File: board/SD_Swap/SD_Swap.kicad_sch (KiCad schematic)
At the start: 43 parts, among them J1 USB_C, Q1 Q_Dual_PNP_PNP_E1B1C2E2B2C1, U1 74LVC2G14, U2 RTS5306E, U3 PCB_SD, U4 93AAxxAT, U5 TS3A27518ERTW, U6 SD_SOCKET, U7 AZ1117-3.3, Y1 12MHz

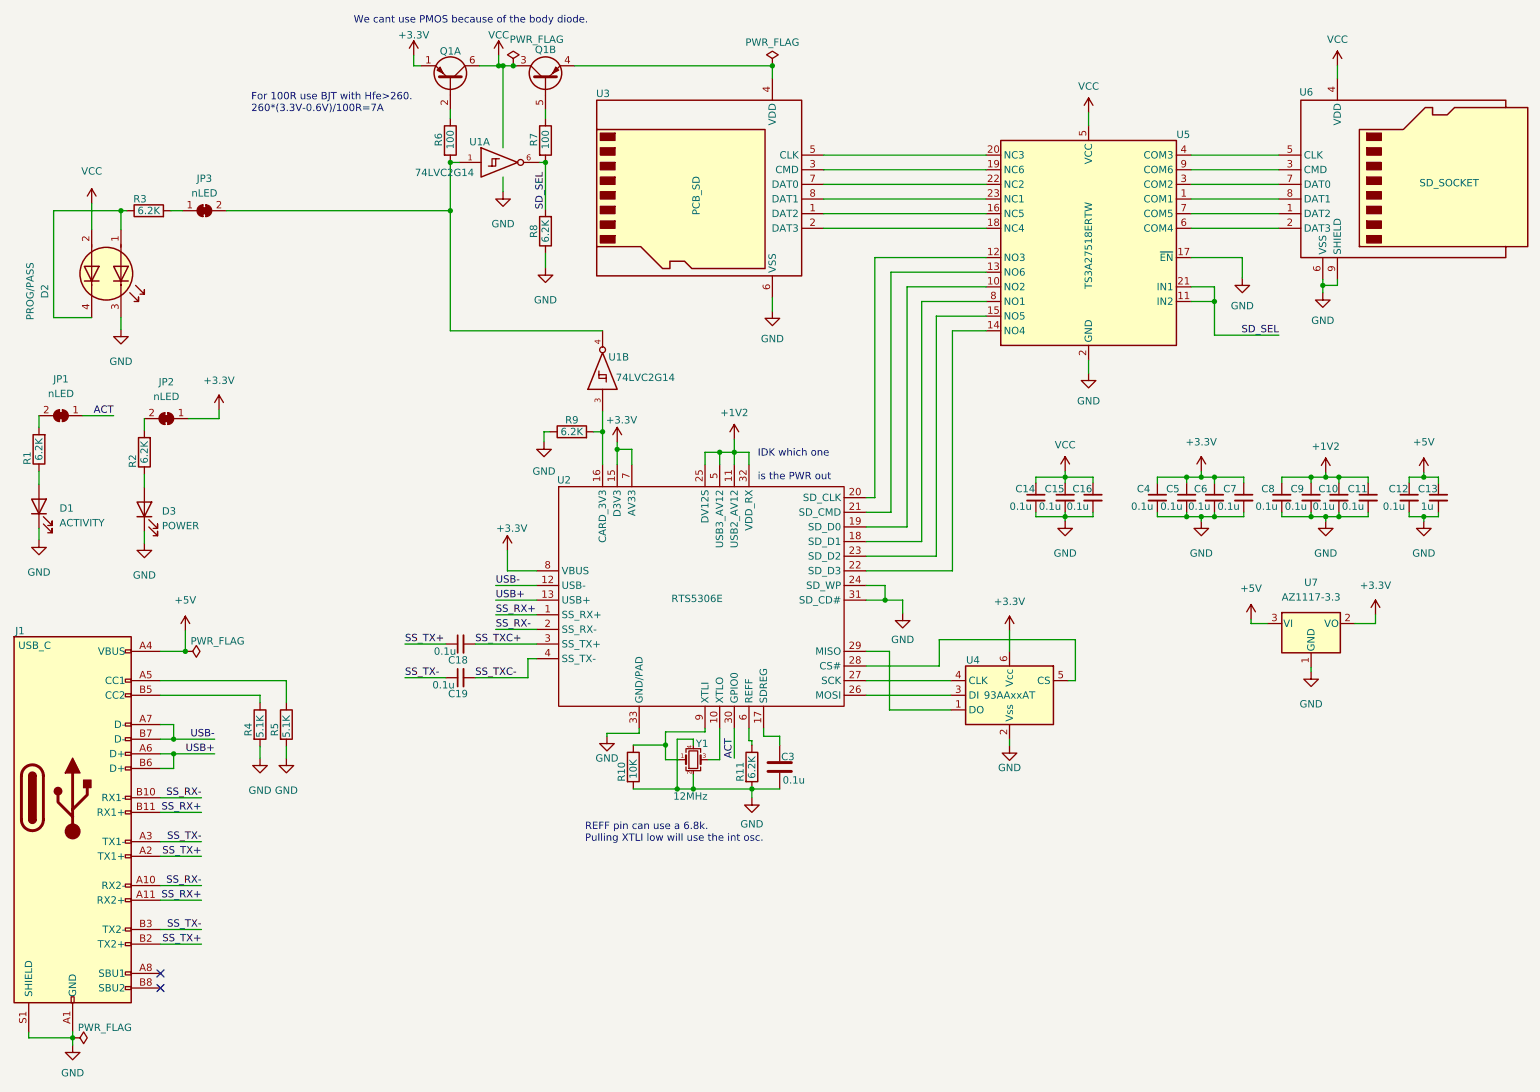
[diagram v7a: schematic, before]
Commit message: update sch to use diodes to power the inverter
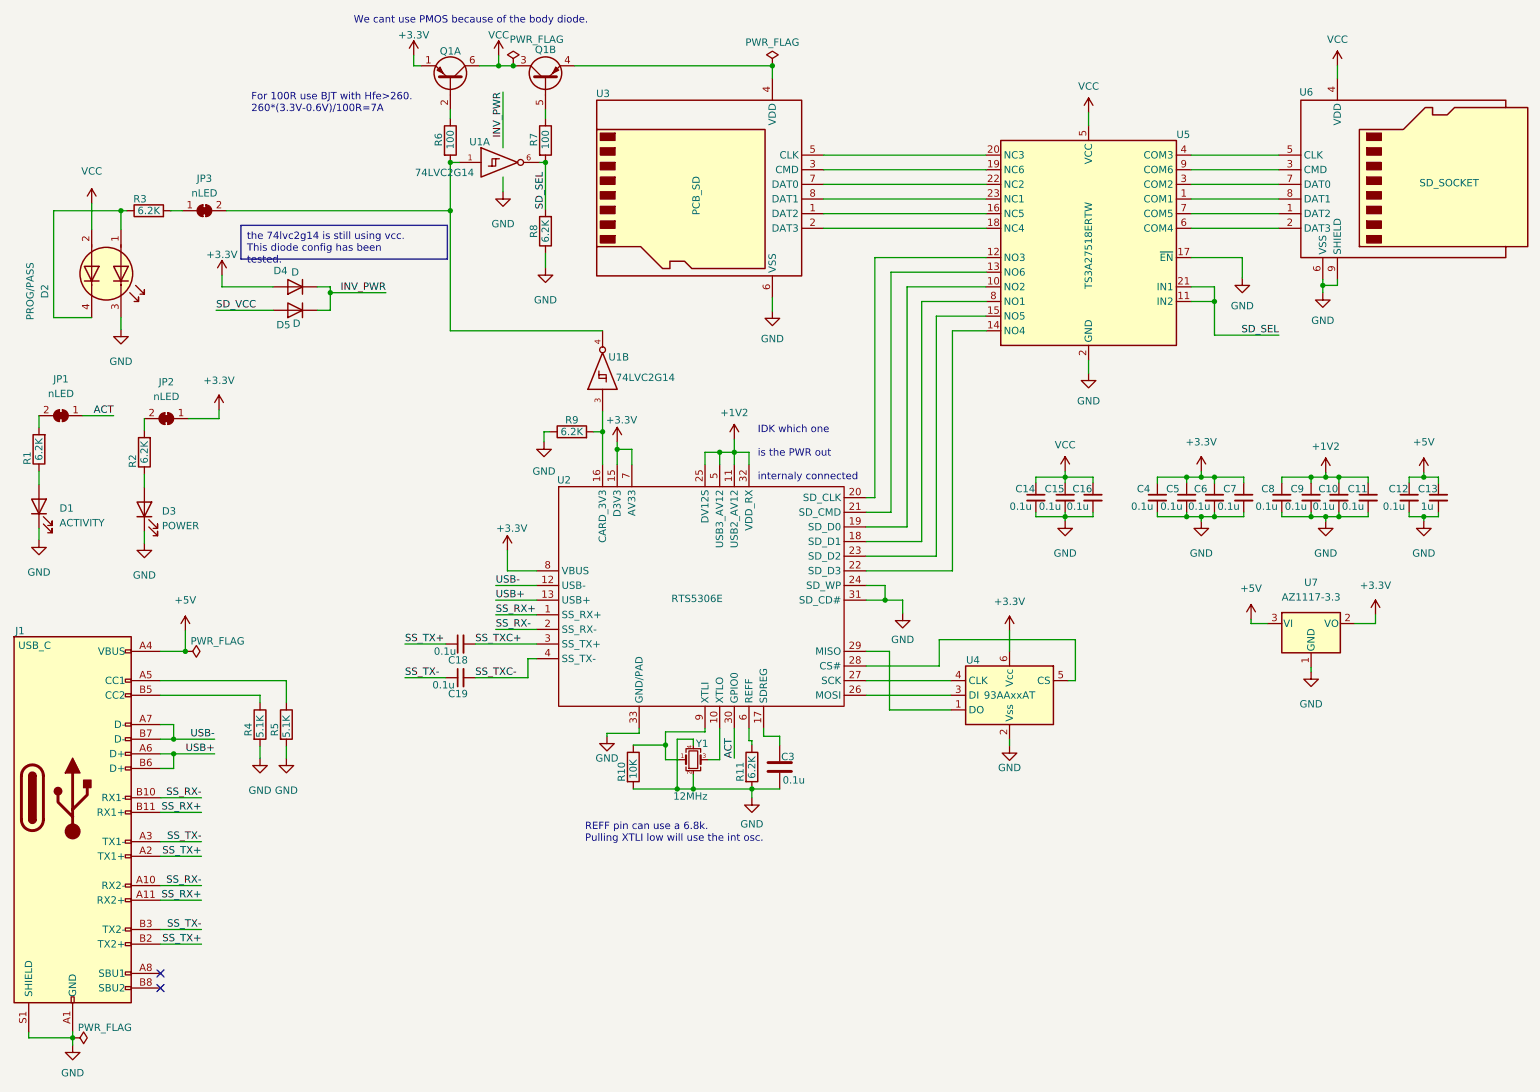
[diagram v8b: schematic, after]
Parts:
- added D4, D5: D, Diode_SMD:D_0201_0603Metric, symbol Device:D
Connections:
- net +3.3V: now also D4.2 (A)
- net VCC: now also D4.1 (K), D5.1 (K)
- new net SD_VCC: D5.2 (A)
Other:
- note added: "IDK which one is the PWR out internaly connected"
- note removed: "IDK which one is the PWR out"
